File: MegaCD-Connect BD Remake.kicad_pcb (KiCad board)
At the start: 2 copper layers, 98 x 44 mm, 17 parts, among them IC1 GAL22V10, IC2 74HC374, IC3 74HC374, IC4 74LS10, IC5 74HC245, IC6 74HC245, J1 MD EXPANSION, J2 CD EXPANSION, J3 TREE HOUSE

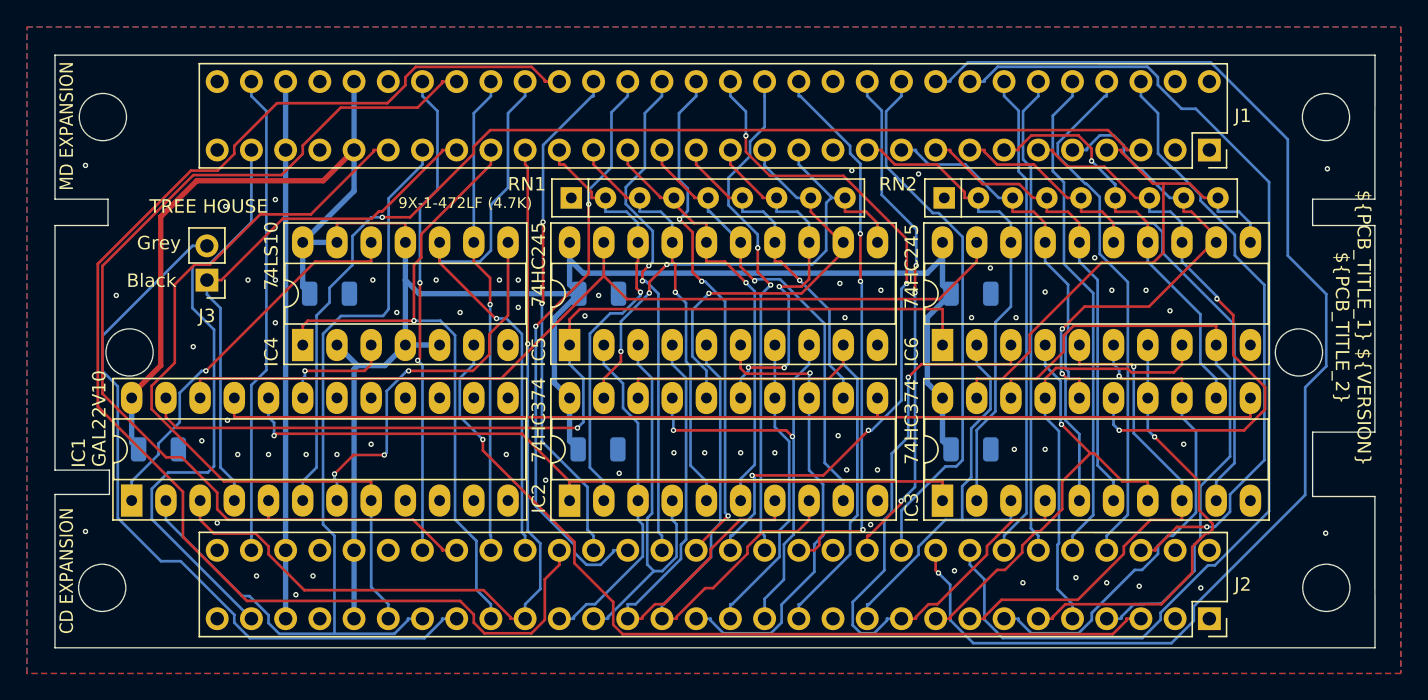
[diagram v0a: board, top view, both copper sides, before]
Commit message: Update PCB to Version 2.1 * Moved /TRDIR from pin 23 to pin 15 * Added GAL20V8 Logic * Updated Labels for Tree House Connection, TH1 and TH2 * Added an iBom * Updated the ReadMe
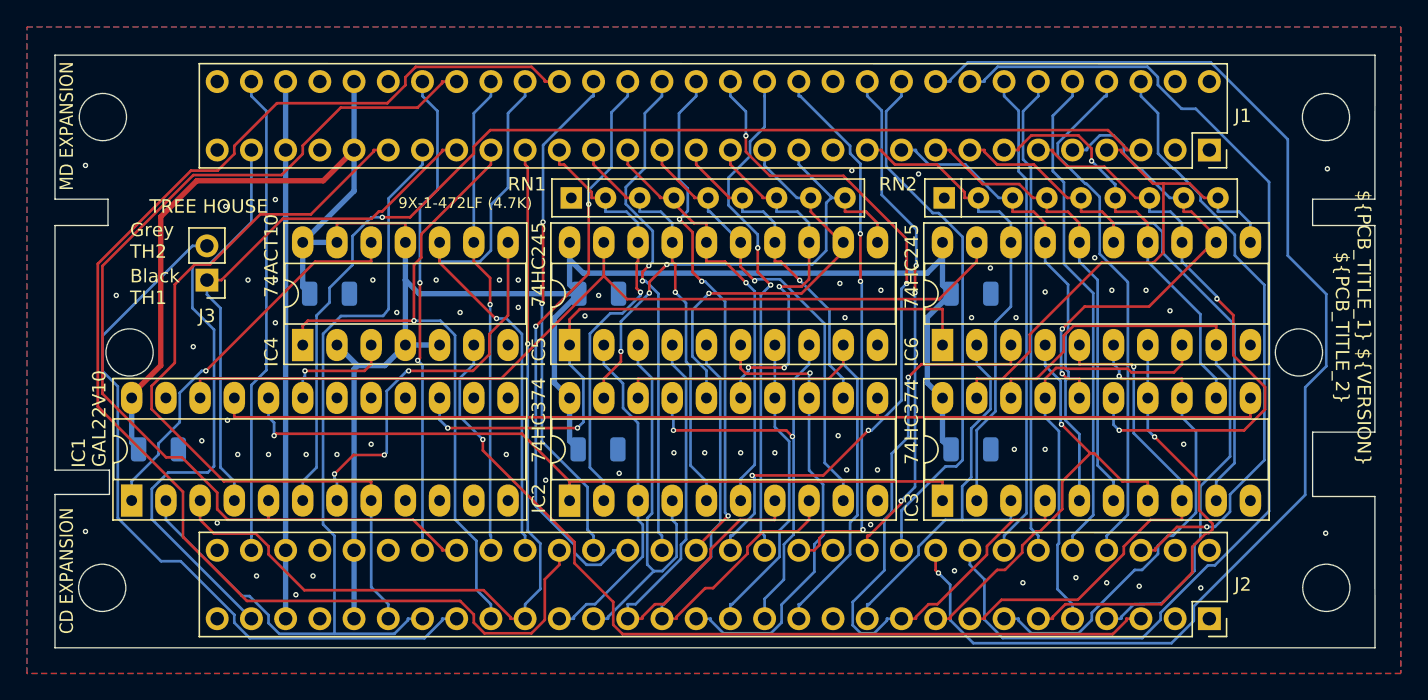
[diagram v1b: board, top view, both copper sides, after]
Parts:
- IC4: value 74LS10 -> 74ACT10
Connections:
- IC1 pad 15: GND -> TR_DIR
- IC1 pad 23: TR_DIR -> unconnected-(IC1-IO1-Pad23)
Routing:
- net TR_DIR: track 71.7 -> 51.5 mm, vias 1 -> 2
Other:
- board text added: "Black TH1"
- board text added: "Grey TH2"
- board text removed: "Black"
- board text removed: "Grey"
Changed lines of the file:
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@@
     )
   )
-  (property "DATE" "05/2023")
+  (property "DATE" "06/2023")
   (property "PCB_TITLE_1" "MegaCD")
   (property "PCB_TITLE_2" "Connect BD Remake")
   (property "PCB_TITLE_3" "Chrissy @chris_jh")
   (property "PCB_TITLE_4" "Board Folk Team")
-  (property "VERSION" "v2.0")
+  (property "VERSION" "v2.1")
   (net 0 "")
   (net 1 "VCC")
@@
   (net 83 "unconnected-(J2-Pin_a27-Pada27)")
   (net 84 "unconnected-(J2-Pin_b27-Padb27)")
+  (net 85 "unconnected-(IC1-IO1-Pad23)")
   (footprint "Package_DIP:DIP-20_W7.62mm_Socket_LongPads" (layer "F.Cu")
     (at 145.288 94.615 90)
@@
         (effects (font (size 1 1) (thickness 0.15)))
     )
-    (fp_text value "74LS10" (at 6.615 -2.33 90) (layer "F.SilkS")
+    (fp_text value "74ACT10" (at 6.615 -2.33 90) (layer "F.SilkS")
         (effects (font (size 1 1) (thickness 0.15)))
     )
@@
       (net 2 "GND") (pinfunction "IO10") (pintype "passive"))
     (pad "15" thru_hole oval (at 7.62 22.86 90) (size 2.4 1.6) (drill 0.8) (layers "*.Cu" "*.Mask")
-      (net 2 "GND") (pinfunction "IO9") (pintype "passive"))
+      (net 18 "TR_DIR") (pinfunction "IO9") (pintype "passive"))
     (pad "16" thru_hole oval (at 7.62 20.32 90) (size 2.4 1.6) (drill 0.8) (layers "*.Cu" "*.Mask")
       (net 11 "unconnected-(IC1-IO8-Pad16)") (pinfunction "IO8") (pintype "passive+no_connect"))
@@
       (net 17 "TR_CE") (pinfunction "IO2") (pintype "passive"))
     (pad "23" thru_hole oval (at 7.62 2.54 90) (size 2.4 1.6) (drill 0.8) (layers "*.Cu" "*.Mask")
-      (net 18 "TR_DIR") (pinfunction "IO1") (pintype "passive"))
+      (net 85 "unconnected-(IC1-IO1-Pad23)") (pinfunction "IO1") (pintype "passive+no_connect"))
     (pad "24" thru_hole oval (at 7.62 0 90) (size 2.4 1.6) (drill 0.8) (layers "*.Cu" "*.Mask")
       (net 1 "VCC") (pinfunction "VCC") (pintype "power_in"))
@@
     (effects (font (size 1 1) (thickness 0.15)) (justify bottom mirror))
   )
-  (gr_text "Grey" (at 113.157 87.63) (layer "F.SilkS")
+  (gr_text "Grey\nTH2" (at 112.649 88.265) (layer "F.SilkS")
     (effects (font (size 1 1) (thickness 0.15)) (justify left bottom))
   )
-  (gr_text "${PCB_TITLE_1} ${VERSION}\n${PCB_TITLE_2}" (at 202.057 93.345 -90) (layer "F.SilkS")
+  (gr_text "${PCB_TITLE_1} ${VERSION}\n${PCB_TITLE_2}" (at 202.057 93.345 270) (layer "F.SilkS")
     (effects (font (size 1 1) (thickness 0.15)) (justify bottom))
   )
-  (gr_text "Black" (at 112.395 90.424) (layer "F.SilkS")
+  (gr_text "Black\nTH1" (at 112.649 91.694) (layer "F.SilkS")
     (effects (font (size 1 1) (thickness 0.15)) (justify left bottom))
   )
@@
   (segment (start 175.514 86.995) (end 175.514 88.4221) (width 0.2) (layer "F.Cu") (net 17))
   (segment (start 147.828 89.4851) (end 149.5523 91.2094) (width 0.2) (layer "F.Cu") (net 17))
-  (segment (start 115.316 98.542) (end 115.316 99.9691) (width 0.2) (layer "F.Cu") (net 18))
   (segment (start 145.288 94.615) (end 145.288 92.71) (width 0.2) (layer "F.Cu") (net 18))
   (segment (start 172.974 91.948) (end 172.974 94.615) (width 0.2) (layer "F.Cu") (net 18))
-  (segment (start 116.1169 100.77) (end 145.8755 100.77) (width 0.2) (layer "F.Cu") (net 18))
+  (segment (start 136.2456 100.7786) (end 145.8669 100.7786) (width 0.2) (layer "F.Cu") (net 18))
   (segment (start 146.05 91.948) (end 172.974 91.948) (width 0.2) (layer "F.Cu") (net 18))
+  (segment (start 145.8669 100.7786) (end 145.8755 100.77) (width 0.2) (layer "F.Cu") (net 18))
   (segment (start 145.288 92.71) (end 146.05 91.948) (width 0.2) (layer "F.Cu") (net 18))
-  (segment (start 115.316 99.9691) (end 116.1169 100.77) (width 0.2) (layer "F.Cu") (net 18))
+  (via (at 136.2456 100.7786) (size 0.4) (drill 0.2) (layers "F.Cu" "B.Cu") (net 18))
   (via (at 145.8755 100.77) (size 0.4) (drill 0.2) (layers "F.Cu" "B.Cu") (net 18))
   (segment (start 145.288 94.615) (end 145.288 96.0421) (width 0.2) (layer "B.Cu") (net 18))
   (segment (start 146.3151 100.3304) (end 146.3151 97.0692) (width 0.2) (layer "B.Cu") (net 18))
+  (segment (start 135.636 98.542) (end 135.636 100.169) (width 0.2) (layer "B.Cu") (net 18))
+  (segment (start 135.636 100.169) (end 136.2456 100.7786) (width 0.2) (layer "B.Cu") (net 18))
   (segment (start 146.3151 97.0692) (end 145.288 96.0421) (width 0.2) (layer "B.Cu") (net 18))
   (segment (start 145.8755 100.77) (end 146.3151 100.3304) (width 0.2) (layer "B.Cu") (net 18))

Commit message: Updated to v2.2
Moved traces near the two middle screws.
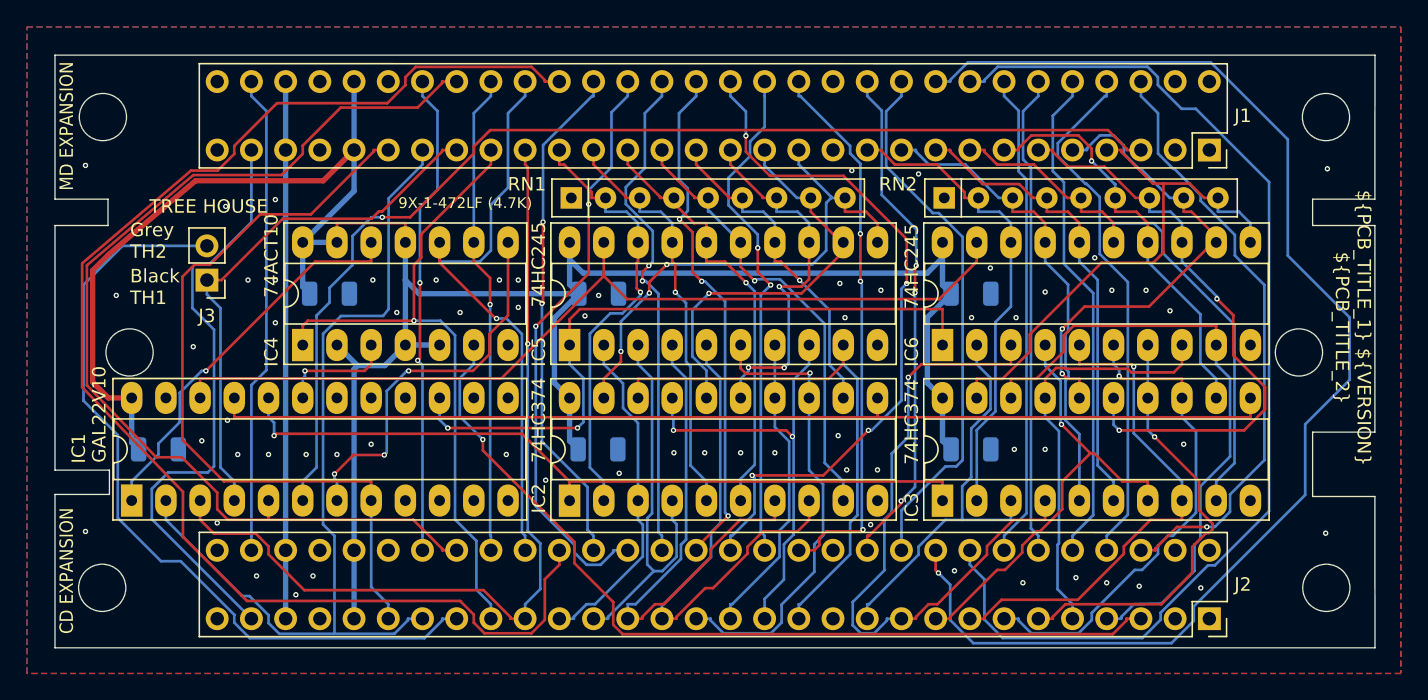
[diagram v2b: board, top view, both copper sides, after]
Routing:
- net ~{CDRAS2}: track 54.4 -> 58.6 mm
- net VCC: track 175.4 -> 179.2 mm
- net FRES: track 59.3 -> 57.4 mm
- net ~{CAS2}: track 75.2 -> 76.9 mm
- net /VA7: track 95.3 -> 96.7 mm
- net /VA17: track 100.6 -> 101.9 mm

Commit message: Updated PCB to v2.3 removed A26 B26 Linking to VCC and back to 9V instead on the CD Side Only.
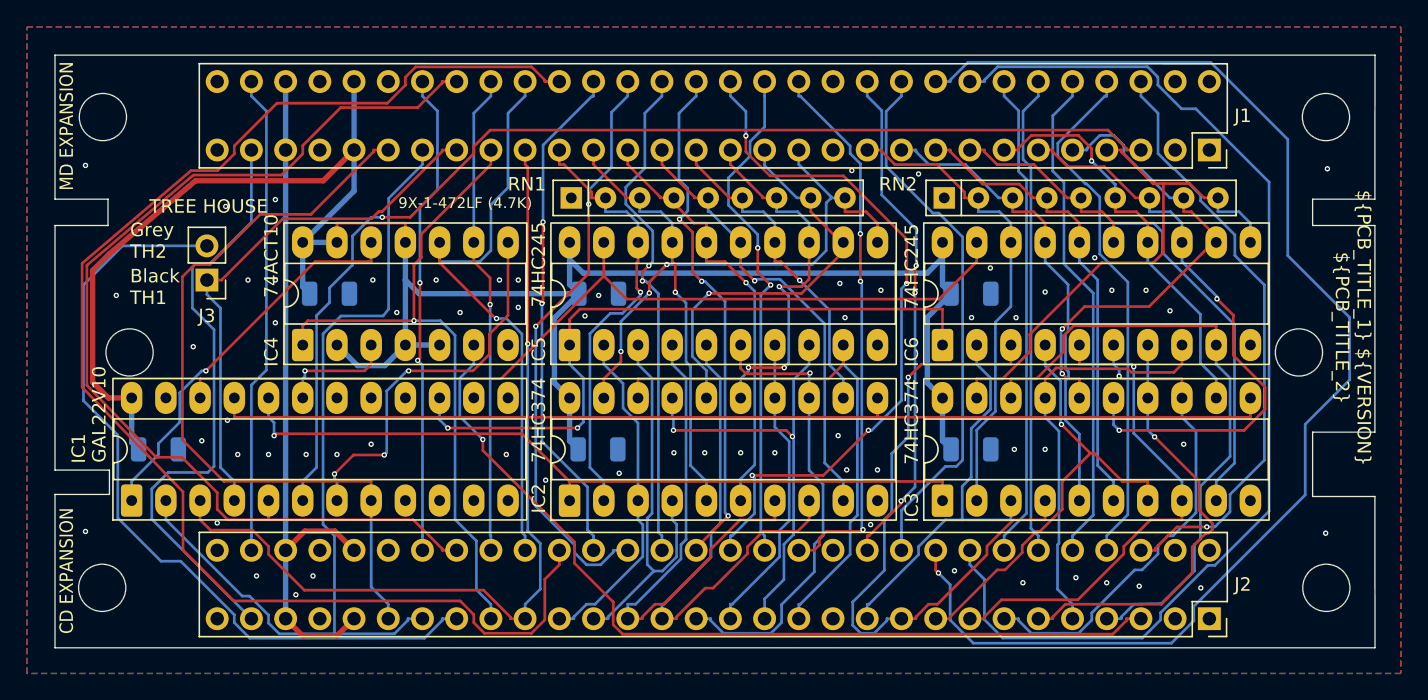
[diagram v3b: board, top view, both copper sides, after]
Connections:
- J2 pad a26: VCC -> +9V
- J2 pad b26: VCC -> +9V
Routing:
- net VCC: track 179.2 -> 160.3 mm
- net +9V: track 39.9 -> 52.3 mm
- net /VA17: track 101.9 -> 102.5 mm
